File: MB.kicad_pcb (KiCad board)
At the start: 4 copper layers, 98.4 x 188.6 mm, 190 parts, among them J100 VCC INPUT, J101 SWITCH ON/OFF, J102 FAN VOLTAGE, J200 Serial Wire Debug, J300 MESA_OUTPUT, J301 TECHO_OUTPUT, J302 MESA_OUTPUT, J303 TECHO_OUTPUT, J304 MESA_OUTPUT, J305 TECHO_OUTPUT, J306 MESA_OUTPUT, J307 TECHO_OUTPUT, J308 MESA_OUTPUT, J309 TECHO_OUTPUT, J400 MESA_OUTPUT, J401 TECHO_OUTPUT, J402 MESA_OUTPUT, J403 TECHO_OUTPUT, J404 MESA_OUTPUT, J405 TECHO_OUTPUT, J406 MESA_OUTPUT, J407 TECHO_OUTPUT, K300 HF49FD/005-1H12T, K301 HF49FD/005-1H12T, K302 HF49FD/005-1H12T, K303 HF49FD/005-1H12T, K304 HF49FD/005-1H12T, K305 HF49FD/005-1H12T, K306 HF49FD/005-1H12T, K307 HF49FD/005-1H12T, K308 HF49FD/005-1H12T, K309 HF49FD/005-1H12T, K400 HF49FD/005-1H12T, K401 HF49FD/005-1H12T, K402 HF49FD/005-1H12T, K403 HF49FD/005-1H12T, K404 HF49FD/005-1H12T, K405 HF49FD/005-1H12T, K406 HF49FD/005-1H12T, K407 HF49FD/005-1H12T, Q100 WST4045, Q300 MMBT3904, Q301 MMBT3904, Q302 MMBT3904, Q303 MMBT3904, Q304 MMBT3904, Q305 MMBT3904, Q306 MMBT3904, Q307 MMBT3904, Q308 MMBT3904, Q309 MMBT3904, Q400 MMBT3904, Q401 MMBT3904, Q402 MMBT3904, Q403 MMBT3904, Q404 MMBT3904, Q405 MMBT3904, Q406 MMBT3904, Q407 MMBT3904, U100 LMR23625CFDDA, U101 AMS1117-3.3, U200 STM32F103C8Tx, Y200 16MHz

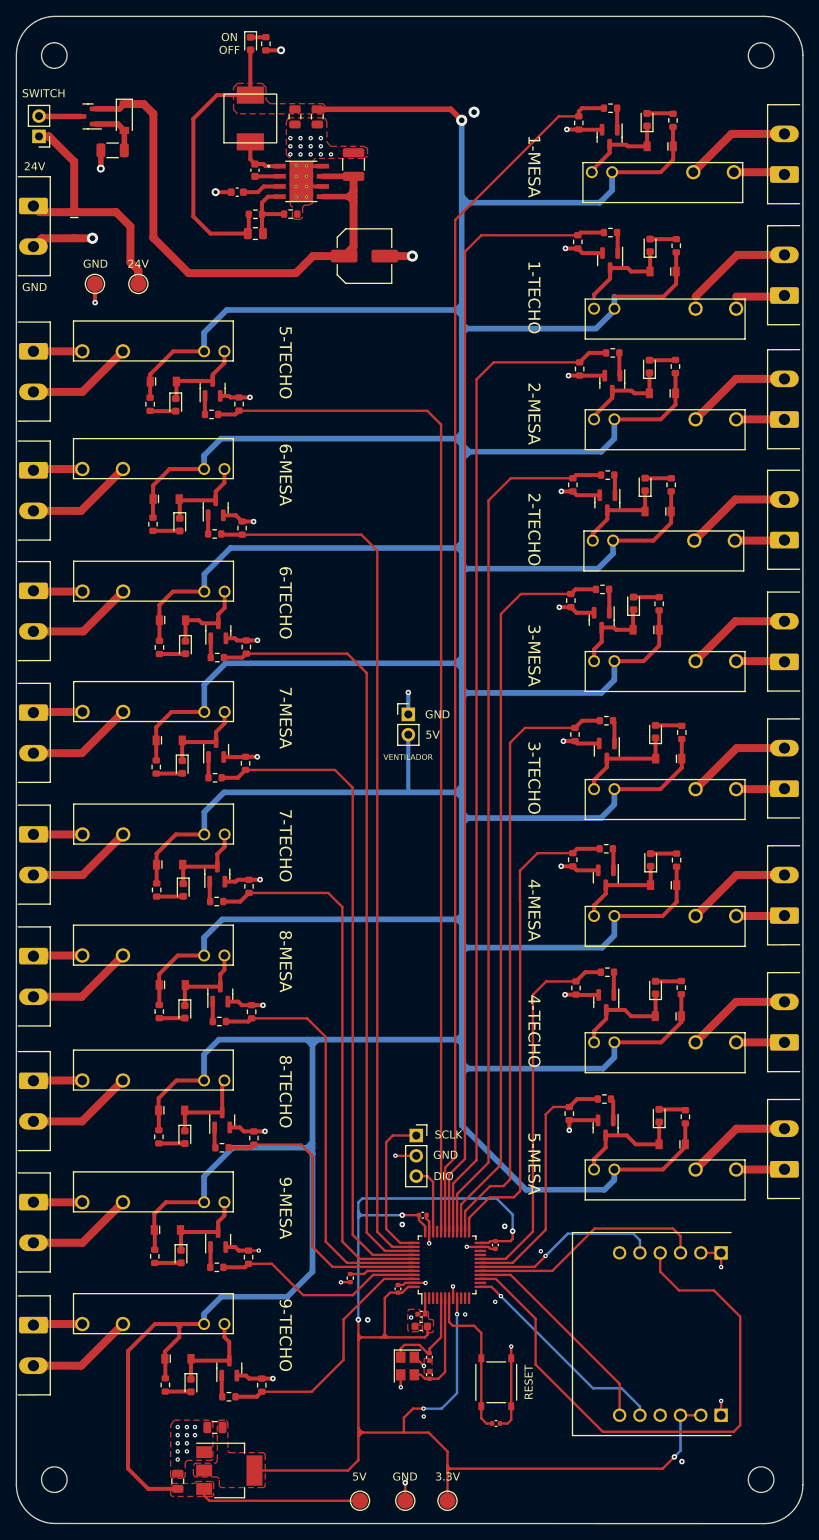
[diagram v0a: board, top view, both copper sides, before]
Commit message: change switch position and thermal vias of LMR
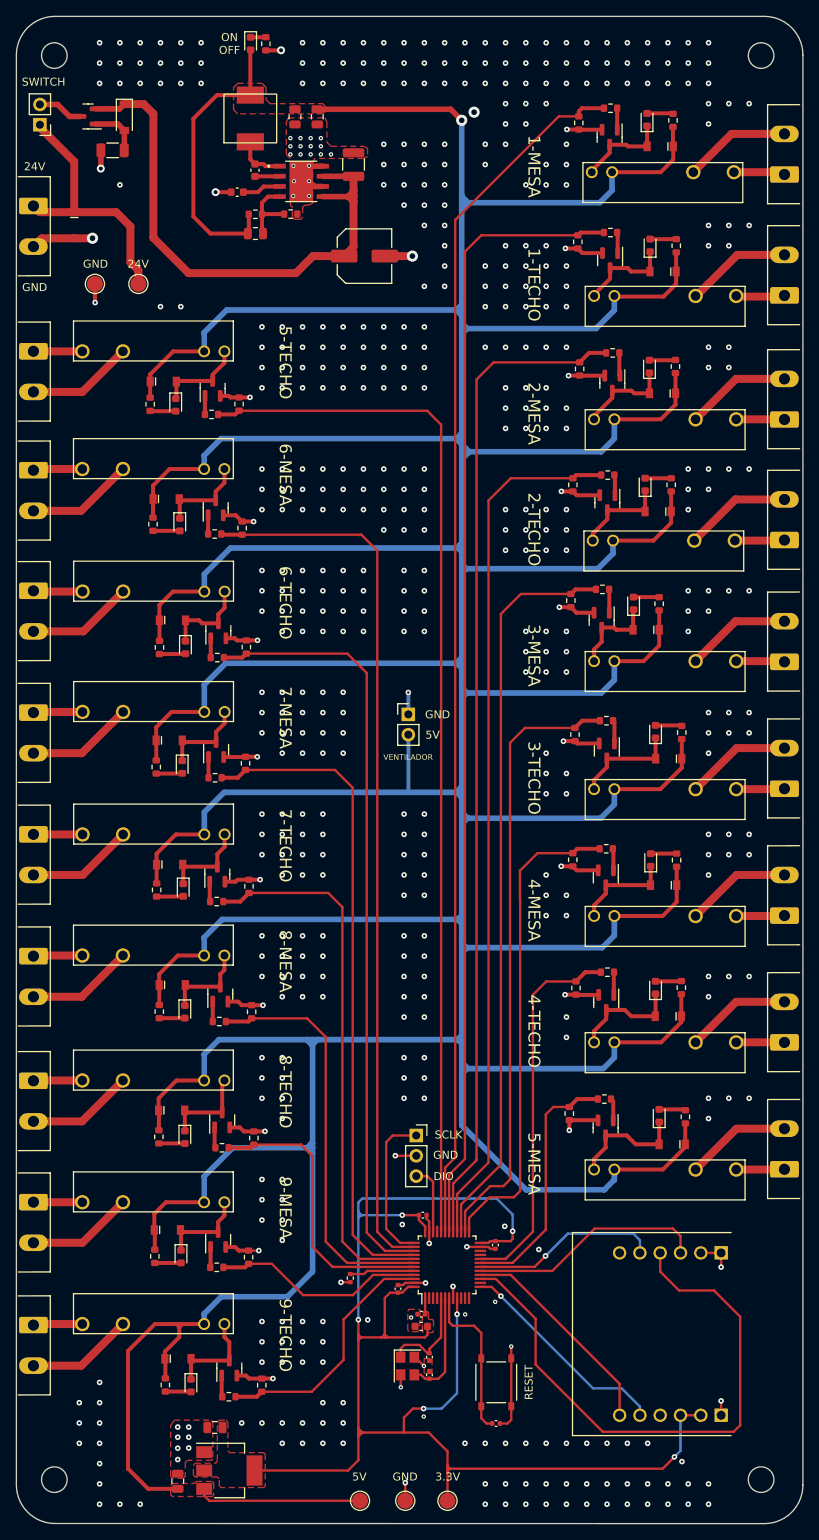
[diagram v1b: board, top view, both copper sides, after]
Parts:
- moved K400 1.59 mm to (169.8, 86.0)
- moved J101 1.46 mm to (91.6, 63.6)
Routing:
- net /POWER/V_INPUT: track 32.8 -> 33.5 mm
- net GND: track 146.2 -> 145.9 mm, vias 71 -> 564
